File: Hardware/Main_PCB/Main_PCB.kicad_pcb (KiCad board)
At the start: 4 copper layers, 65 x 49 mm, 86 parts, among them J201 Sonar, J601 Conn_01x08_Pin, J602 Conn_01x03_Pin, J603 Servo con, P301 USB_C_Plug_USB2.0, SW301 TL3342F160QG_TR, SW302 TL3342F160QG_TR, U201 TUSS4470TRTJT, U301 RP2040, U302 W25Q128JVS, U401 TPS62170DSG, U402 TPS61175PWPR, U403 BD50FD0WFP2-E2, U501 ICM-42688-P, U601 NRF24L01, U602 SN74LV1T34DBV, Y301 12Mhz

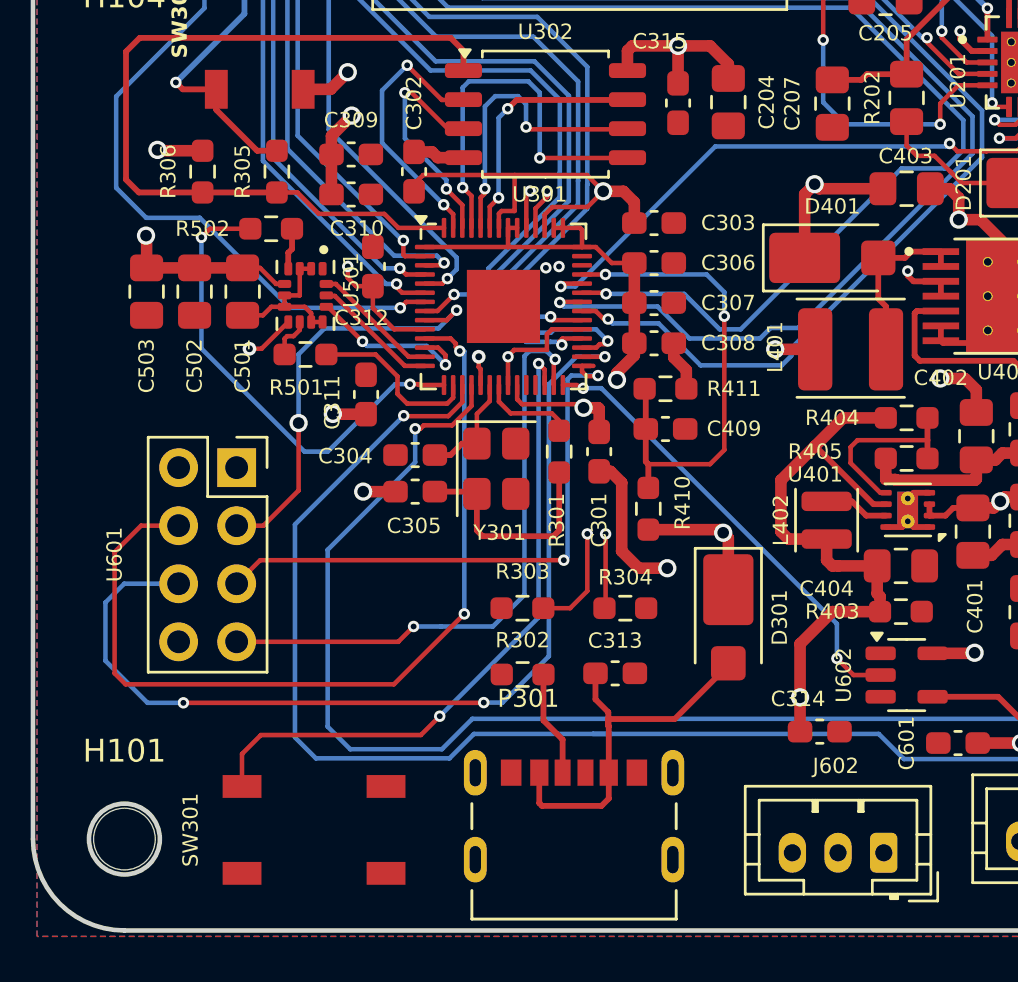
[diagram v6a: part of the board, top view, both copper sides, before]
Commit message: Updated the PCB with new USB-C
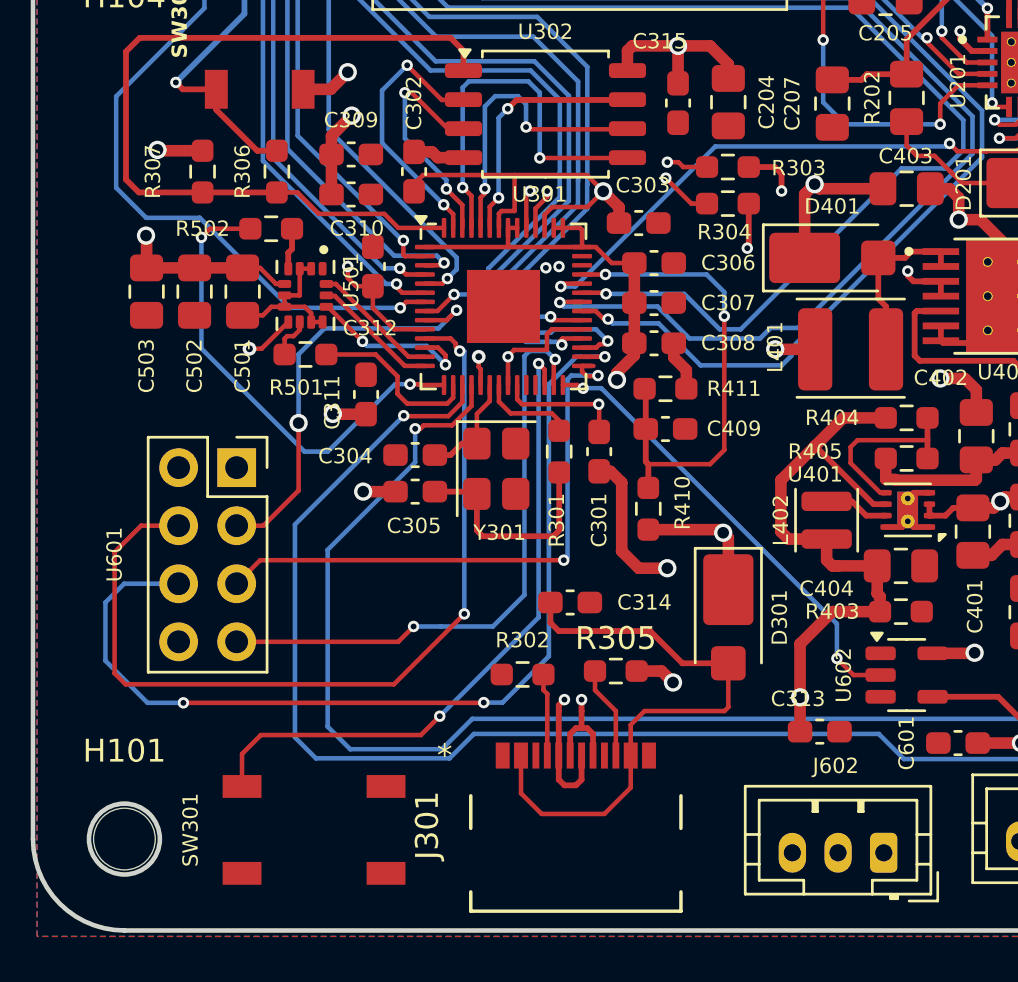
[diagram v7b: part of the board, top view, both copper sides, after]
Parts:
- removed P301: USB_C_Plug_USB2.0, MainPCB:CUI_UJC-HP-3-SMT-TR
- added J301: 2171790001, MainPCB:2171790001_MOL, F.Cu at (87.2, 98.2)
- added R305: 5.1k, Resistor_SMD:R_0603_1608Metric_Pad0.98x0.95mm_HandSolder, F.Cu at (89.0, 91.2)
- moved R304 19.9 mm to (93.9, 70.8), turned to 180 degrees
- moved R303 19.8 mm to (93.9, 69.2)
- moved C314 3.67 mm to (87.0, 88.2)
- moved C303 0.67 mm to (90.0, 71.7)
- renumbered C314 to C313, C313 to C314, R304 to R303, R303 to R304, R305 to R306, R306 to R307
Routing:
- net Net-(J301-DP1): track 0.00 -> 32.5 mm, vias 0 -> 2
- net Net-(J301-DN1): track 0.00 -> 30.9 mm, vias 0 -> 2
- net /RP2040/D-: track 37.3 -> 10.1 mm
- net /RP2040/D+: track 37.3 -> 10.4 mm
- net Net-(D301-A): track 16.9 -> 26.1 mm
- net Net-(J301-CC2): track 0.00 -> 4.07 mm
- net GND: track 54.6 -> 56.4 mm, vias 9 -> 10
- net +1V1: track 37.3 -> 36.0 mm
- net Net-(J301-CC1): track 4.64 -> 3.62 mm
- net /OUT3: track 124.1 -> 123.3 mm

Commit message: V1.1 of the MainPCB
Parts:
- added C208: 1u, Capacitor_SMD:C_0603_1608Metric_Pad1.08x0.95mm_HandSolder, F.Cu at (116.2, 58.3)
- added R301: 10k, Capacitor_SMD:C_0603_1608Metric_Pad1.08x0.95mm_HandSolder, F.Cu at (70.2, 94.0)
- C203: value 20n -> 22n; footprint Capacitor_SMD:C_0805_2012Metric_Pad1.18x1.45mm_HandSolder -> Capacitor_SMD:C_0603_1608Metric_Pad1.08x0.95mm_HandSolder
- C206: value 2u -> 1u
- L401: footprint MainPCB:L_33uH -> MainPCB:VLCF4018
- Y301: value 12Mhz -> 12MHz
- moved C406 15.7 mm to (102.2, 82.3), turned to 180 degrees
- moved C402 10.8 mm to (98.2, 72.3), turned to 180 degrees
- moved C401 9.42 mm to (95.3, 83.8), turned to 90 degrees
- moved C311 9.07 mm to (86.5, 82.5), turned to -90 degrees
- moved C403 8.89 mm to (110.0, 73.4)
- moved R404 8.80 mm to (101.6, 89.0), turned to 0 degrees
- moved C405 8.38 mm to (98.6, 80.2), turned to 180 degrees
- moved R407 8.37 mm to (106.0, 82.0), turned to 180 degrees
- moved C205 7.70 mm to (107.8, 58.5), turned to 180 degrees
- moved R402 7.45 mm to (111.6, 78.7)
- moved C207 7.42 mm to (103.2, 60.8), turned to 180 degrees
- moved R405 6.52 mm to (98.1, 87.4)
- moved D401 5.41 mm to (103.8, 73.8), turned to 180 degrees
- moved C404 5.01 mm to (98.3, 82.8), turned to 180 degrees
- moved U401 3.80 mm to (98.1, 85.2), turned to 0 degrees
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- renumbered R301 to R302, R302 to R303, R303 to R304, R304 to R305, R305 to R306, R306 to R307, R307 to R308
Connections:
- net Net-(J301-DN1) renamed /RP2040/Data-
- net Net-(J301-DP1) renamed /RP2040/Data+
- C206 pad 1: Net-(U201-VDRV) -> GND
- C206 pad 2: GND -> Net-(U201-VDRV)
- Y301 pad 2: Net-(C305-Pad1) -> GND
- Y301 pad 3: (no net) -> Net-(C305-Pad1)
- Y301 pad 4: (no net) -> GND
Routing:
- net /OUT3: track 123.3 -> 82.9 mm
- net /RP2040/GPIO3: track 59.7 -> 35.0 mm, vias 4 -> 2
- net /RP2040/GPIO0: track 53.6 -> 29.0 mm
- net +3.3V: track 84.2 -> 65.6 mm
- net /BEMF: track 45.5 -> 28.3 mm, vias 1 -> 3
- net /AHS: track 49.8 -> 36.0 mm, vias 1 -> 2
- net GND: track 56.4 -> 43.1 mm, vias 10 -> 62
- net VDC: track 23.8 -> 10.8 mm, vias 6 -> 1
- net +12V: track 14.3 -> 2.62 mm, vias 4 -> 1
- net /ALS: track 51.0 -> 40.1 mm, vias 1 -> 2
- net Net-(U402-FB): track 10.5 -> 0.00 mm
- net Net-(U402-SS): track 9.66 -> 0.00 mm
- net /BHS: track 48.8 -> 40.0 mm, vias 1 -> 2
- net Net-(U401-FB): track 8.05 -> 0.00 mm
- net Net-(D401-A): track 7.64 -> 0.00 mm
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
